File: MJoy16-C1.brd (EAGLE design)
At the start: 98.7 x 63.5 mm, 35 parts, among them U1 MEGA16-P, X1 12MHz

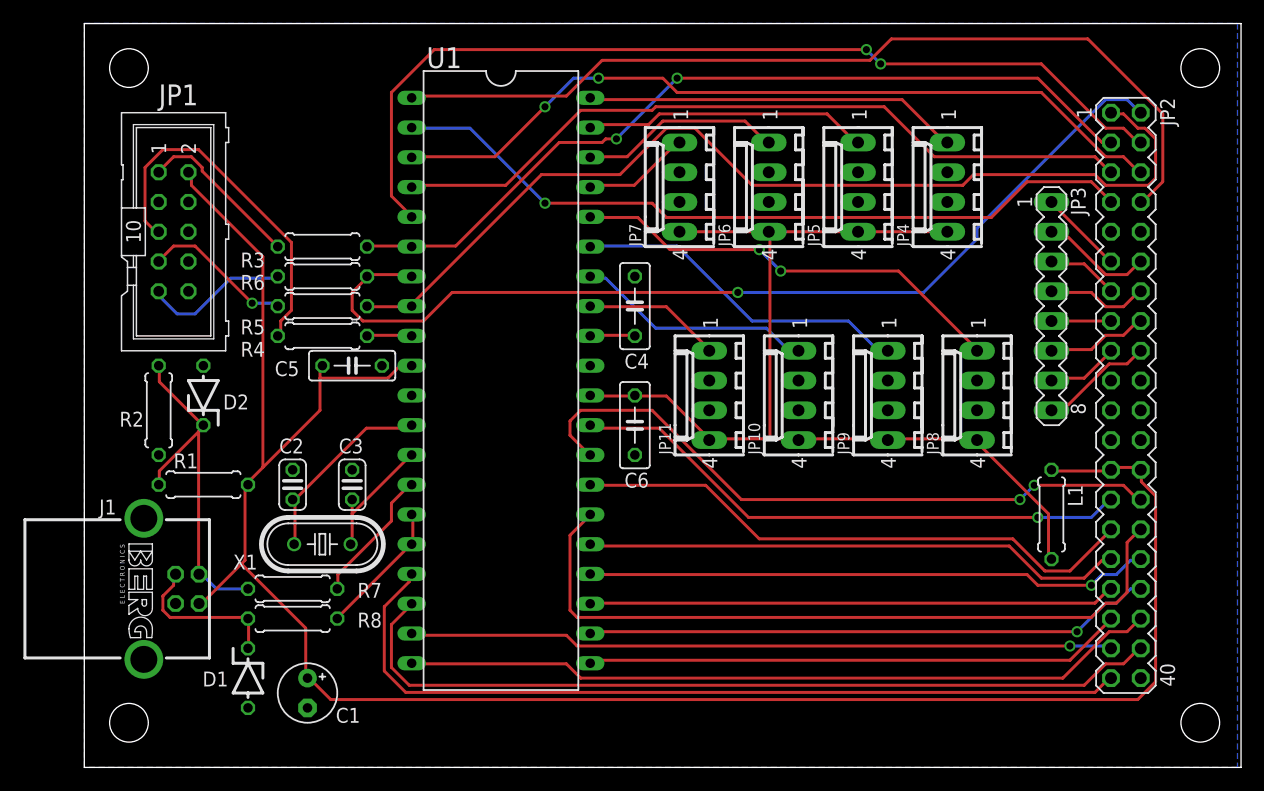
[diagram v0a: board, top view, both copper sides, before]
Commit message: added text for original design by Mindaugas Milasauskas
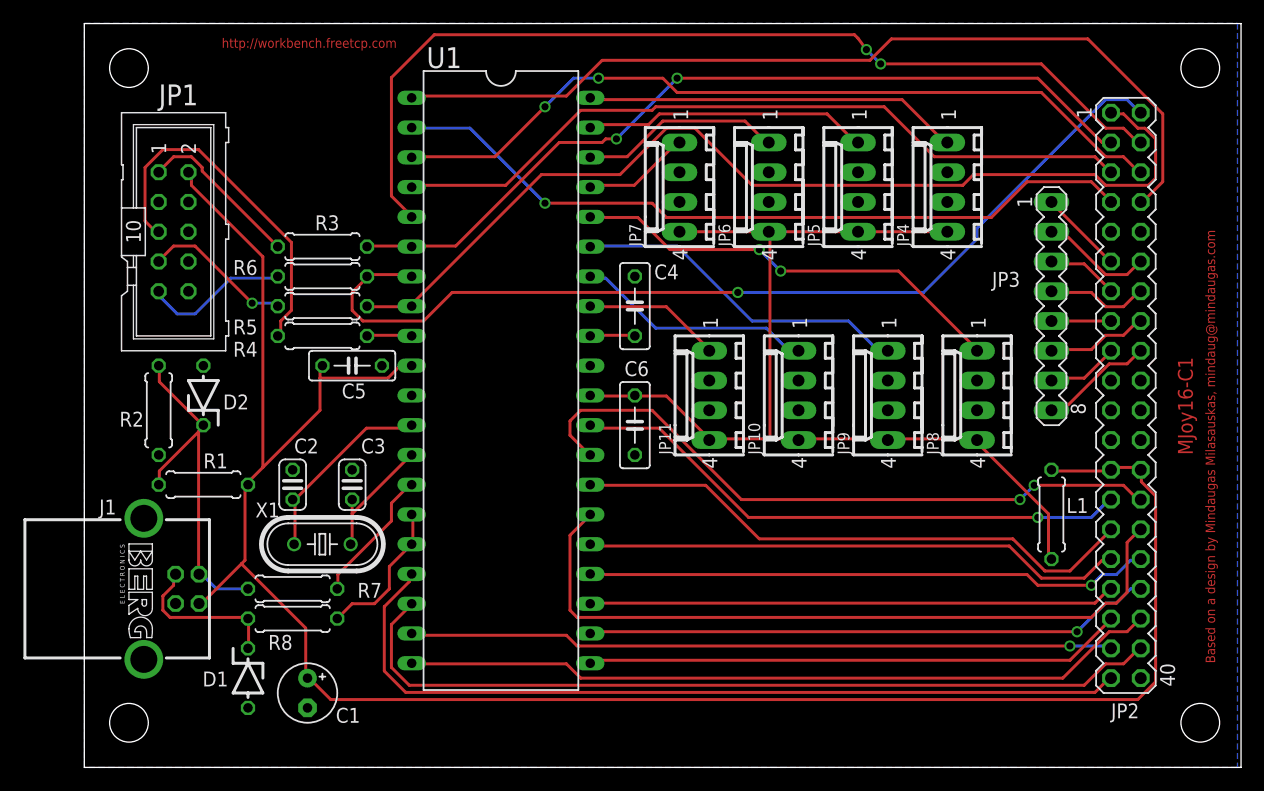
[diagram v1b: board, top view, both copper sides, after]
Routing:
- net PB4: track 80.1 -> 82.0 mm
- net N$10: track 11.6 -> 12.7 mm
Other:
- board text added: "Based on a design by Mindaugas Milasauskas, mindaug@mindaugas.com"
- board text added: "MJoy16-C1"
- board text added: "http://workbench.freetcp.com"
